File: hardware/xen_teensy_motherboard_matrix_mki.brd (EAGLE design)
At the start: 69.9 x 110.5 mm, 222 parts, among them IC1 TL074PW, IC10 MCP4351-104E_ST, IC11 MCP4351-104E_ST, IC12 MCP4351-104E_ST, IC13 MCP4351-104E_ST, IC14 MCP4351-104E_ST, IC15 MCP4351-104E_ST, IC16 MCP4351-104E_ST, IC17 MCP4351-104E_ST, IC2 TL074PW, IC3 MCP6004, IC4 MCP4351-104E_ST, IC5 TL074PW, IC6 TEENSY41-OUTER, IC7 R-78E5.0-0.5, IC8 LM4040-5V, IC9 LD2981 3.3V

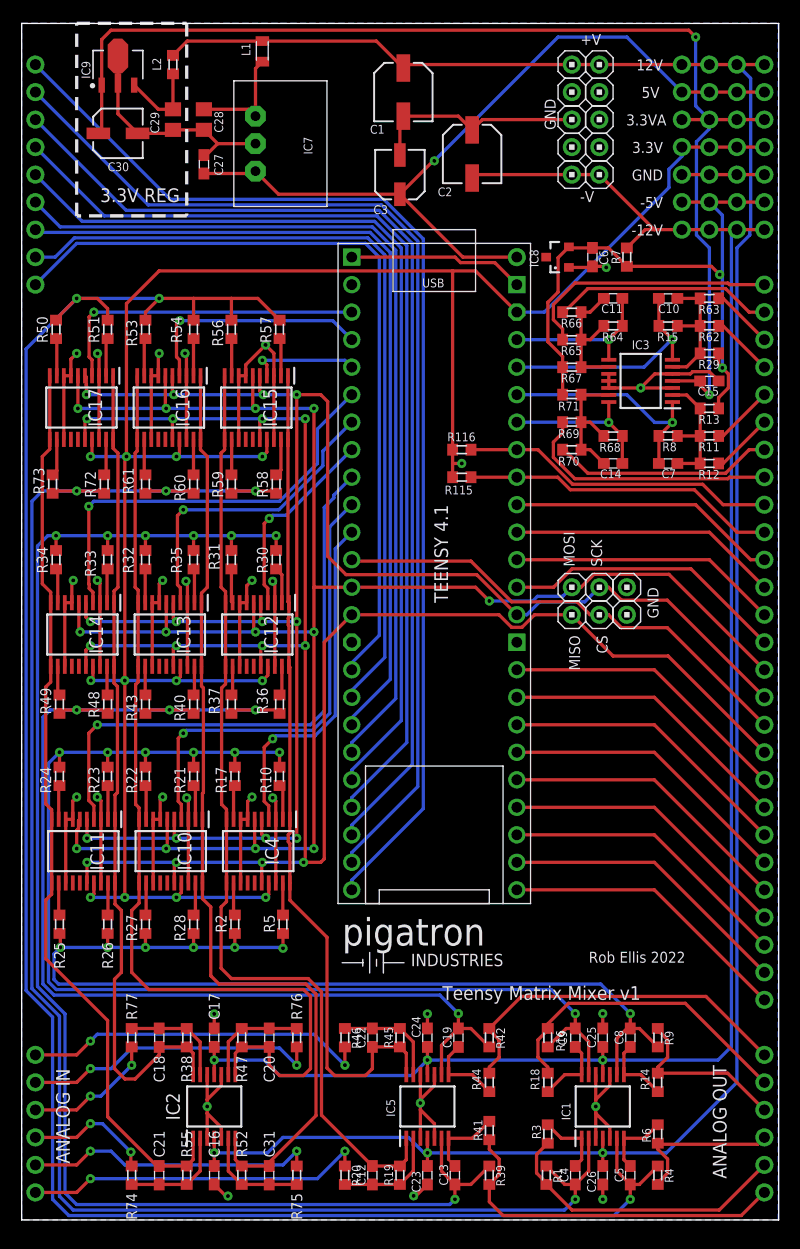
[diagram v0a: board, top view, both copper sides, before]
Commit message: add offset to input and output voltages
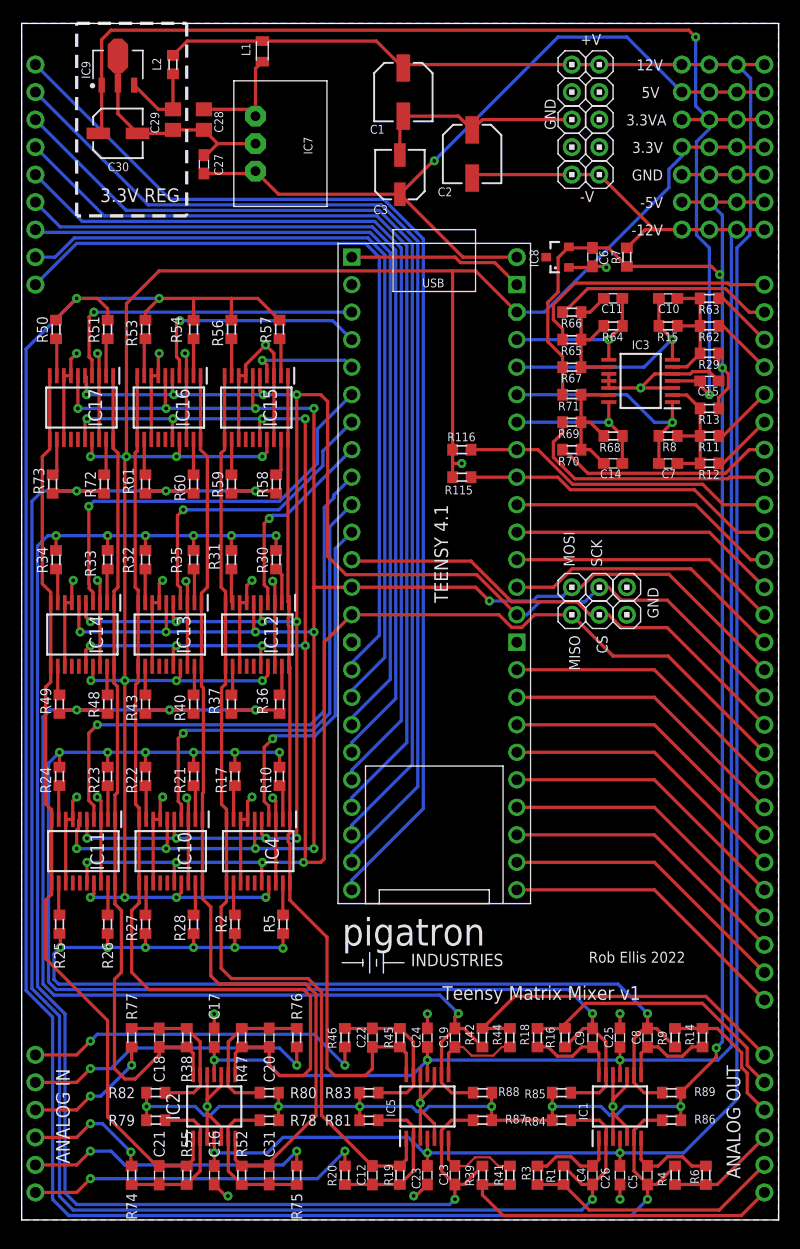
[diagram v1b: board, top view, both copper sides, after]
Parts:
- added R78, R79, R80, R81, R82, R83, R84, R85, R86, R87, R88, R89: 100k, resistors:R0603
- R1, R16, R20, R39, R4, R42, R46, R74, R75, R76, R77, R9: value 100k -> 200k
- R10, R17, R19, R2, R21, R22, R23, R24, R25, R26, R27, R28, R30, R31, R32, R33, R34, R35, R36, R37, R38, R40, R43, R45, R47, R48, R49, R5, R50, R51, R52, R53, R54, R55, R56, R57, R58, R59, R60, R61, R72, R73: value 100k -> 47k
- moved R6 5.85 mm to (63.2, 4.13)
- moved R14 5.84 mm to (62.9, 16.8)
- moved R44 4.55 mm to (45.1, 16.8)
- moved R41 4.55 mm to (45.1, 4.13)
- moved R18 4.24 mm to (47.6, 16.8)
- moved R3 3.93 mm to (47.6, 4.13)
- moved R4 1.59 mm to (60.3, 4.13)
- moved R9 1.59 mm to (60.3, 16.8)
- moved C25 1.59 mm to (55.2, 16.8)
- moved C26 1.59 mm to (55.2, 4.13)
- moved C4 1.59 mm to (52.7, 4.13)
- moved C5 1.59 mm to (57.8, 4.13)
- moved C8 1.59 mm to (57.8, 16.8)
- moved C9 1.59 mm to (52.7, 16.8)
- moved IC1 1.59 mm to (55.2, 10.5)
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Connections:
- net -5VREF: now also R78.1, R79.1, R80.1, R81.1, R82.1, R83.1, R84.1, R85.1, R86.1, R87.1, R88.1, R89.1
- net N$12: now also R80.2
- net N$2: now also R82.2
- net N$20: now also R81.2
- net N$28: now also R78.2
- net N$48: now also R83.2
- net N$50: now also R79.2
- net OUT1: now also R85.2
- net OUT2: now also R89.2
- net OUT3: now also R87.2
- net OUT4: now also R88.2
- net OUT5: now also R86.2
- net OUT6: now also R84.2
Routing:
- net -5VREF: track 59.6 -> 194.4 mm, vias 2 -> 9
- net OUT6: track 158.2 -> 164.4 mm
- net OUT1: track 109.5 -> 115.6 mm
- net OUT2: track 95.8 -> 101.1 mm
- net OUT5: track 183.3 -> 188.7 mm
- net N$7: track 14.7 -> 10.1 mm
- net N$48: track 9.86 -> 14.4 mm
- net N$20: track 9.86 -> 14.4 mm
- net N$50: track 9.86 -> 14.4 mm
- net N$2: track 9.86 -> 14.4 mm
- net N$28: track 9.86 -> 14.1 mm
- net N$12: track 9.86 -> 14.1 mm
- net N$4: track 27.4 -> 23.7 mm
- net OUT4: track 108.0 -> 111.7 mm
- net OUT3: track 138.1 -> 141.5 mm
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
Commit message: buffer calibration voltage
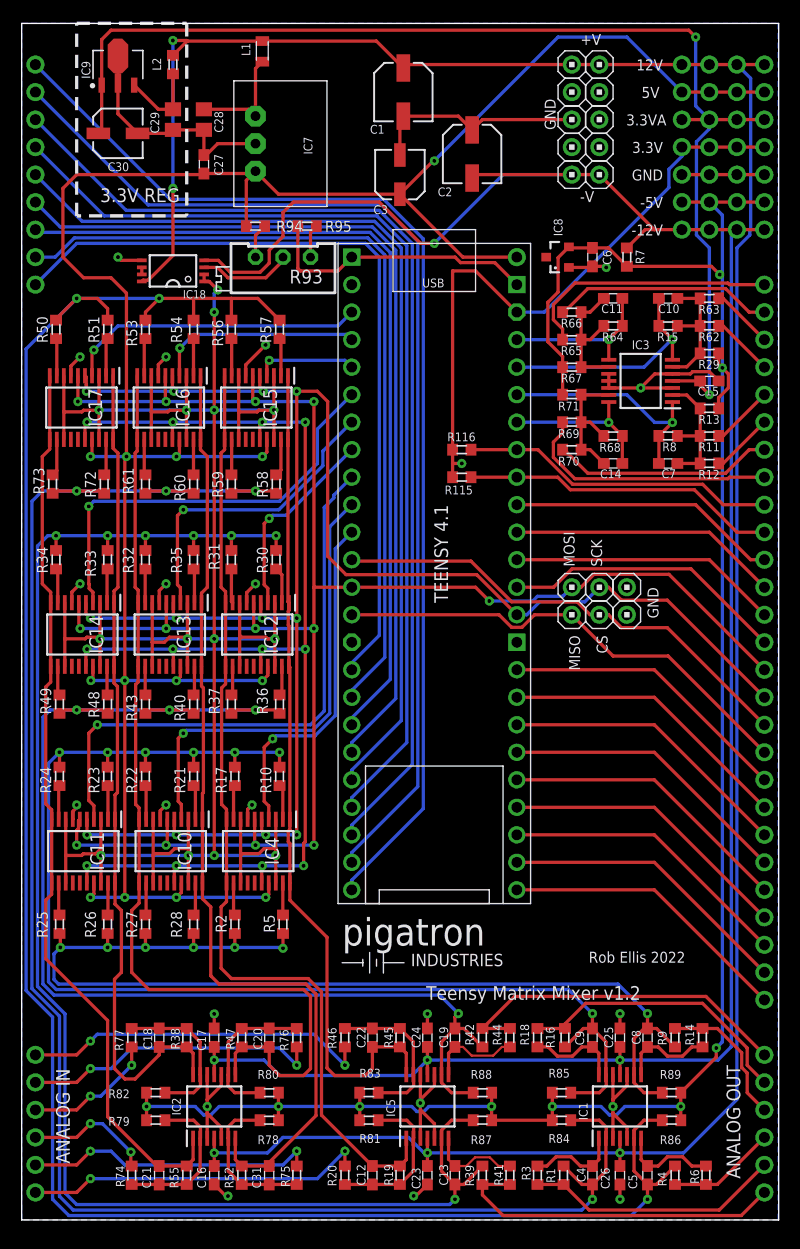
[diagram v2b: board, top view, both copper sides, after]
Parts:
- added IC18: TL072W, ic_analogue:TSSOP08
- added R93: 100k, resistors:TRIMMER/64B
- added R94, R95: 47k, resistors:R0603
- R84, R85, R87: value 100k -> 16.6k
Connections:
- removed net N$74: IC6.3V3-1
- new net N$21: IC18.6, IC18.7
- new net N$43: R93.1, R95.2
- new net N$49: R93.3, R94.1
- new net N$5: IC10.13, IC10.18, IC10.3, IC10.8, IC11.13, IC11.18, IC11.3, IC11.8, IC12.13, IC12.18, IC12.3, IC12.8, IC13.13, IC13.18, IC13.3, IC13.8, IC14.13, IC14.18, IC14.3, IC14.8, IC15.13, IC15.18, IC15.3, IC15.8, IC16.13, IC16.18, IC16.3, IC16.8, IC17.13, IC17.18, IC17.3, IC17.8, IC18.1, IC18.2, IC4.13, IC4.18, IC4.3, IC4.8
- new net N$9: IC18.3, R93.2
- new net SDO: IC10.16, IC11.16, IC12.16, IC13.16, IC14.16, IC15.16, IC16.16, IC17.16, IC4.16
- net +12V: now also IC18.8
- net -12V: now also IC18.4
- net 3.3V: no longer IC10.17, IC11.17, IC12.17, IC13.17, IC14.17, IC15.17, IC16.17, IC17.17, IC4.17
- net 5V: now also IC10.17, IC11.17, IC12.17, IC13.17, IC14.17, IC15.17, IC16.17, IC17.17, IC4.17, R94.2
- net PE: now also IC18.5, R95.1; no longer IC10.13, IC10.18, IC10.3, IC10.8, IC11.13, IC11.18, IC11.3, IC11.8, IC12.13, IC12.18, IC12.3, IC12.8, IC13.13, IC13.18, IC13.3, IC13.8, IC14.13, IC14.18, IC14.3, IC14.8, IC15.13, IC15.18, IC15.3, IC15.8, IC16.13, IC16.18, IC16.3, IC16.8, IC17.13, IC17.18, IC17.3, IC17.8, IC4.13, IC4.18, IC4.3, IC4.8
- net SPI_MISO: no longer IC10.16, IC11.16, IC12.16, IC13.16, IC14.16, IC15.16, IC16.16, IC17.16, IC4.16
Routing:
- net N$5: track 0.00 -> 239.9 mm, vias 0 -> 14
- net 5V: track 74.0 -> 224.4 mm, vias 1 -> 13
- net 3.3V: track 206.2 -> 58.1 mm, vias 13 -> 1
- net SPI_MISO: track 188.8 -> 44.3 mm, vias 12 -> 0
- net PE: track 280.8 -> 158.8 mm, vias 28 -> 21
- net SDO: track 0.00 -> 116.0 mm, vias 0 -> 12
- net -12V: track 165.2 -> 208.5 mm, vias 3 -> 4
- net +12V: track 212.1 -> 237.2 mm, vias 3 -> 5
- net N$9: track 0.00 -> 8.66 mm
- net SPI_MOSI: track 178.4 -> 174.9 mm
- net N$49: track 0.00 -> 3.21 mm
- net N$43: track 0.00 -> 3.08 mm
- net SPI_CS8: track 21.9 -> 19.2 mm
- net SPI_SCK: track 180.6 -> 177.9 mm
- net SPI_CS9: track 30.0 -> 27.7 mm
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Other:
- board text added: "Teensy Matrix Mixer v1.2"
- board text removed: "Teensy Matrix Mixer v1"
